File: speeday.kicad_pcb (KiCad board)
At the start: 4 copper layers, 100 x 100 mm, 284 parts, among them IC10 VNL5090N3-E, IC11 LD29150DT50R, IC12 LD29150DT33R, IC2 Trig Cond Socket, IC3 VNL5090N3-E, IC4 VNL5090N3-E, IC5 VNL5090N3-E, IC6 VNL5090N3-E, IC7 VNL5090N3-E, IC8 VNL5090N3-E, IC9 VNL5090N3-E, J1 MSD-4-A, J10 Conn_02x02_Counter_Clockwise, J11 Conn_02x02_Counter_Clockwise, J12 Conn_01x01, J13 Conn_01x01, J14 Conn_01x01, J15 Conn_01x01, J16 Conn_01x02, J17 Conn_01x02, J18 Conn_01x02, J19 Conn_01x02, J2 Conn_01x02, J20 Conn_01x04, J21 Conn_01x04, J22 Conn_01x04, J23 Conn_01x02, J24 Conn_01x02, J25 Conn_01x08, J26 Conn_01x06, J27 Conn_01x04, J28 12402012E212A, J3 Conn_01x02, J4 Conn_02x02_Counter_Clockwise, J5 Conn_02x02_Counter_Clockwise, J6 Conn_02x02_Counter_Clockwise, J7 Conn_02x02_Counter_Clockwise, J8 Conn_02x02_Counter_Clockwise, J9 Conn_02x02_Counter_Clockwise, Q1 SSM3K357R, Q2 SSM3K357R, Q3 SSM3K357R, Q4 SSM3K357R, SW1 SW_DIP_x01, SW2 SW_DIP_x01, U1 STM32F407VGTx, U10 SP720, U11 MCP2551-I-SN, U12 IXDN602, U13 IXDN602, U2 MCP6004, U3 MCP6002-xMS, U4 MCP6004, U5 MCP6004, U6 TXB0108PW, U7 TXB0108PW, U8 W25Q16JVSS, U9 MPX4250, Y2 Crystal_GND24, Y3 Crystal_GND24

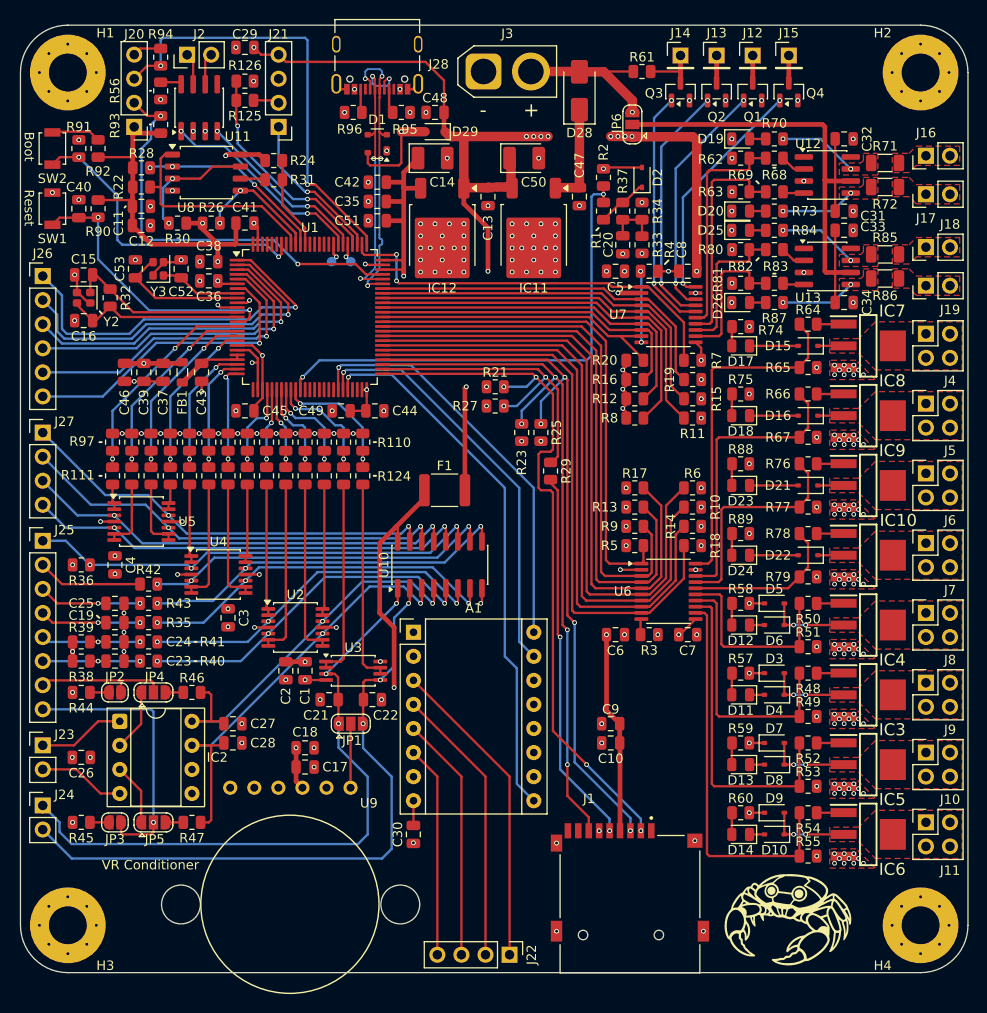
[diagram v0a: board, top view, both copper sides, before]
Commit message: Replace level shifters, rewire for spacing
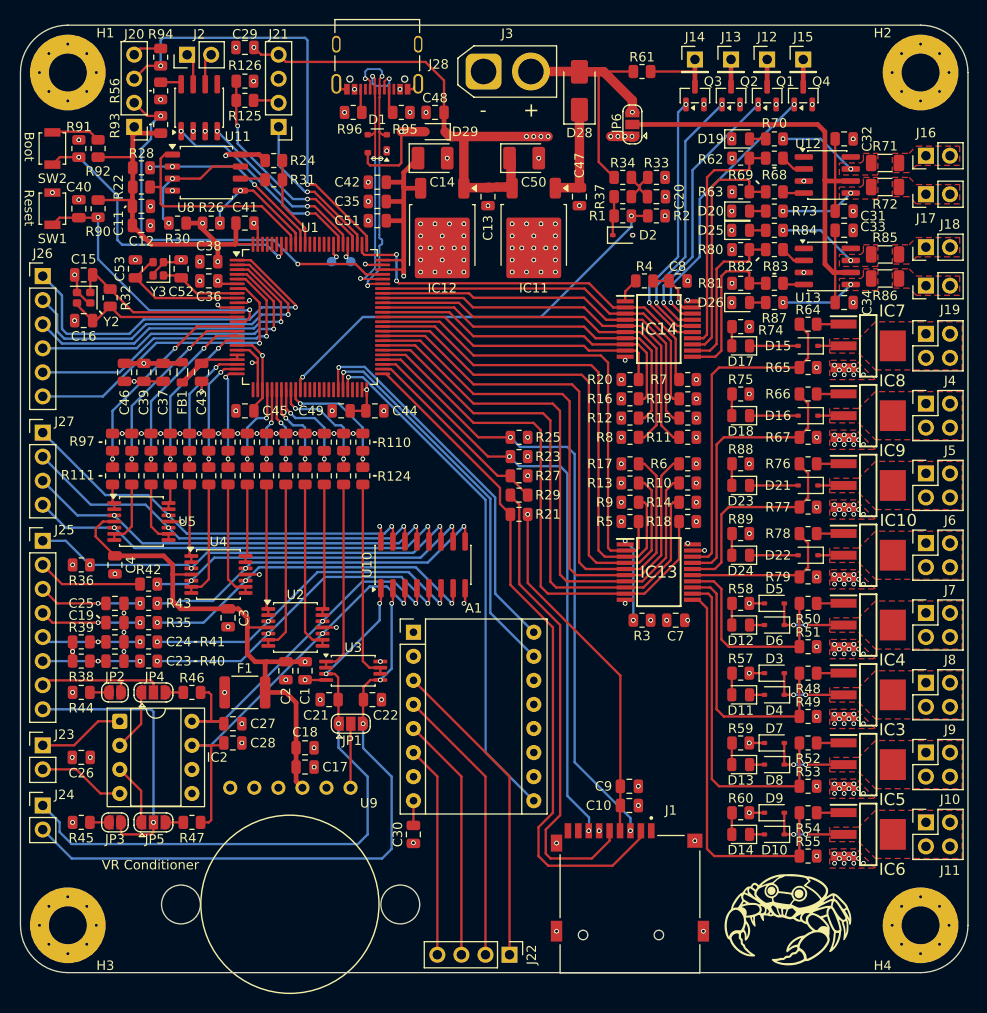
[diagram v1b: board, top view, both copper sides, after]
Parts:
- removed C5, C6: 100nF, Capacitor_SMD:C_0805_2012Metric
- removed U6, U7: TXB0108PW, Package_SO:TSSOP-20_4.4x6.5mm_P0.65mm
- added IC13: SN74AHCT245DBR, Misc:SOP65P780X200-20N, F.Cu at (87.4, 77.7)
- added IC14: SN74AHCT245DBR, Misc:SOP65P780X200-20N, F.Cu at (87.4, 52.1)
- R3: value 1k -> 10k
- moved F1 30.0 mm to (43.7, 90.4)
- moved R21 13.7 mm to (72.6, 71.6), turned to 0 degrees
- moved R27 7.78 mm to (72.6, 67.6), turned to 0 degrees
- moved R33 7.27 mm to (87.1, 36.1), turned to 180 degrees
- moved R2 6.91 mm to (87.1, 40.1), turned to 0 degrees
- moved C10 6.89 mm to (84.3, 102.4), turned to 180 degrees
- moved C9 6.89 mm to (84.3, 100.3), turned to 180 degrees
- moved D2 6.43 mm to (83.6, 42.2), turned to 0 degrees
- moved C20 6.20 mm to (87.1, 38.1), turned to 0 degrees
- moved R29 4.18 mm to (72.6, 69.6), turned to 180 degrees
- moved R34 4.10 mm to (83.6, 36.1), turned to 180 degrees
- moved R10 2.59 mm to (90.4, 68.3)
- moved R13 2.59 mm to (84.3, 68.3)
- moved R17 2.59 mm to (84.3, 66.3)
- moved R18 2.59 mm to (90.4, 72.4)
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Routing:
- net +3.3V: track 259.3 -> 222.8 mm, vias 17 -> 13
- net +5V: track 268.8 -> 239.0 mm, vias 24 -> 16
- net +5VA: track 102.2 -> 80.6 mm, vias 6 -> 7
- net MCU-SPI-SD-CLK: track 33.2 -> 20.9 mm, vias 2 -> 0
- net MCU-SPI-SD-MISO: track 74.5 -> 63.2 mm, vias 4 -> 2
- net MCU-SPI-SD-MOSI: track 76.7 -> 66.6 mm, vias 4 -> 2
- net Net-(J1-CLK): track 39.6 -> 49.4 mm, vias 2 -> 0
- net GND: track 90.2 -> 80.4 mm, vias 274 -> 277
- net Net-(IC13-DIR): track 1.68 -> 9.12 mm, vias 0 -> 2
- net MCU-BAT-REF-IN-A: track 52.8 -> 45.6 mm
- net MCU-HC-2-TRIG-D: track 62.6 -> 56.9 mm
- net MCU-HC-1-TRIG-D: track 63.8 -> 58.8 mm
- net Net-(IC14-DIR): track 7.53 -> 2.62 mm, vias 2 -> 0
- net MCU-BOOST-TRIG-D: track 65.0 -> 60.2 mm
- net MCU-IDLE-TRIG-D: track 66.3 -> 61.7 mm
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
